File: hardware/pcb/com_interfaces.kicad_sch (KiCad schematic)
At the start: 1 part, among them U4 MAX485E

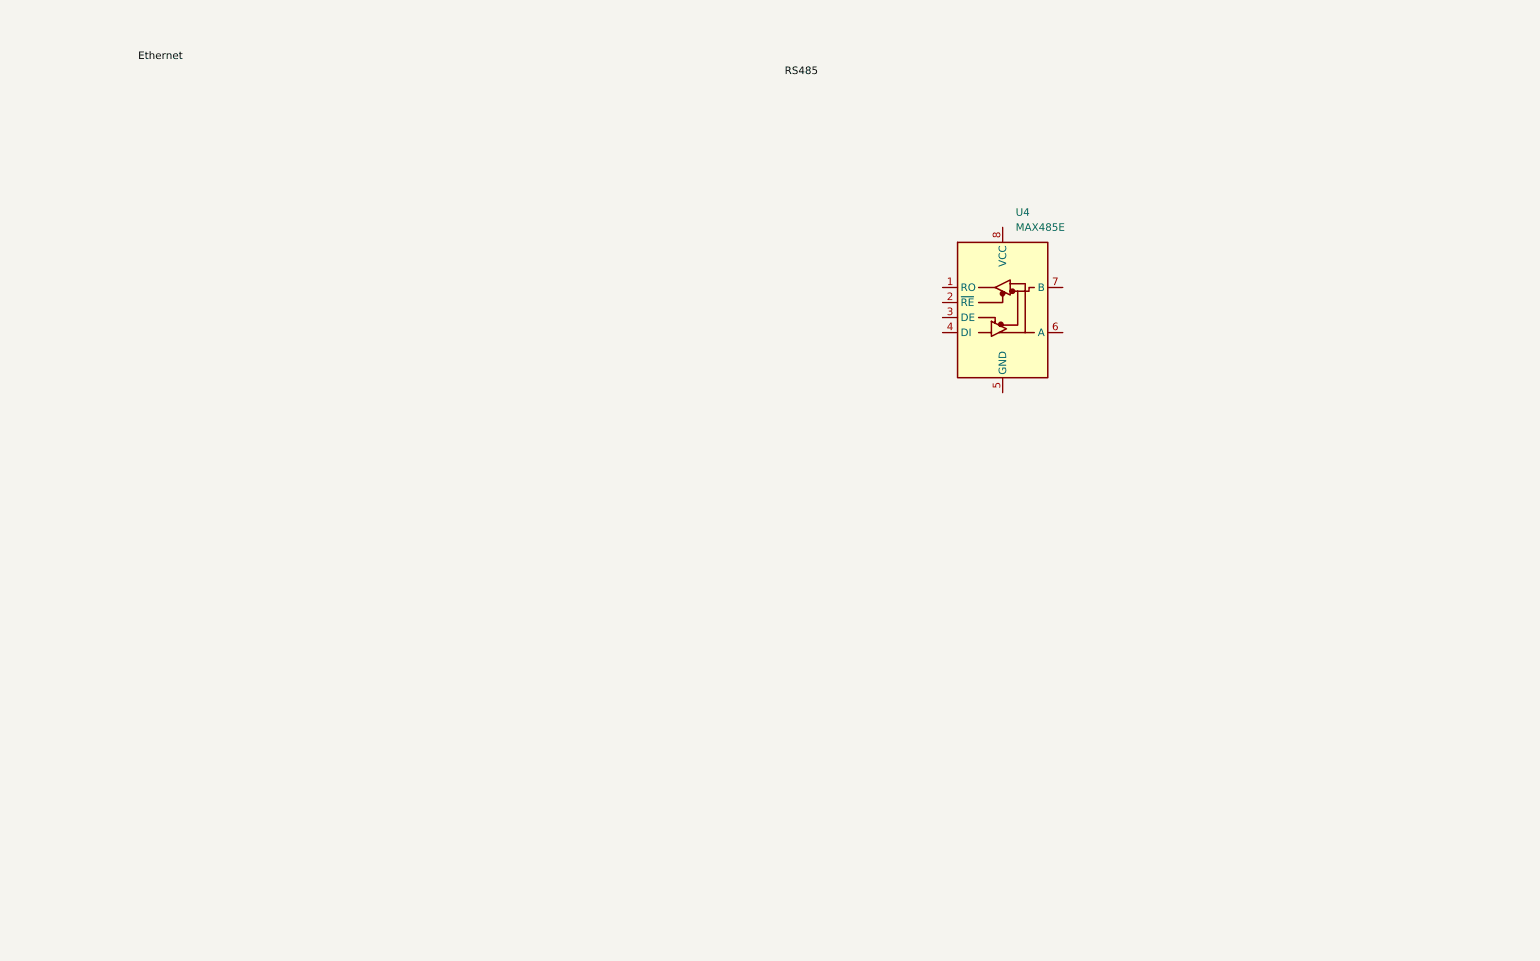
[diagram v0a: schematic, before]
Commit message: draft: Added W5500 Ethernet
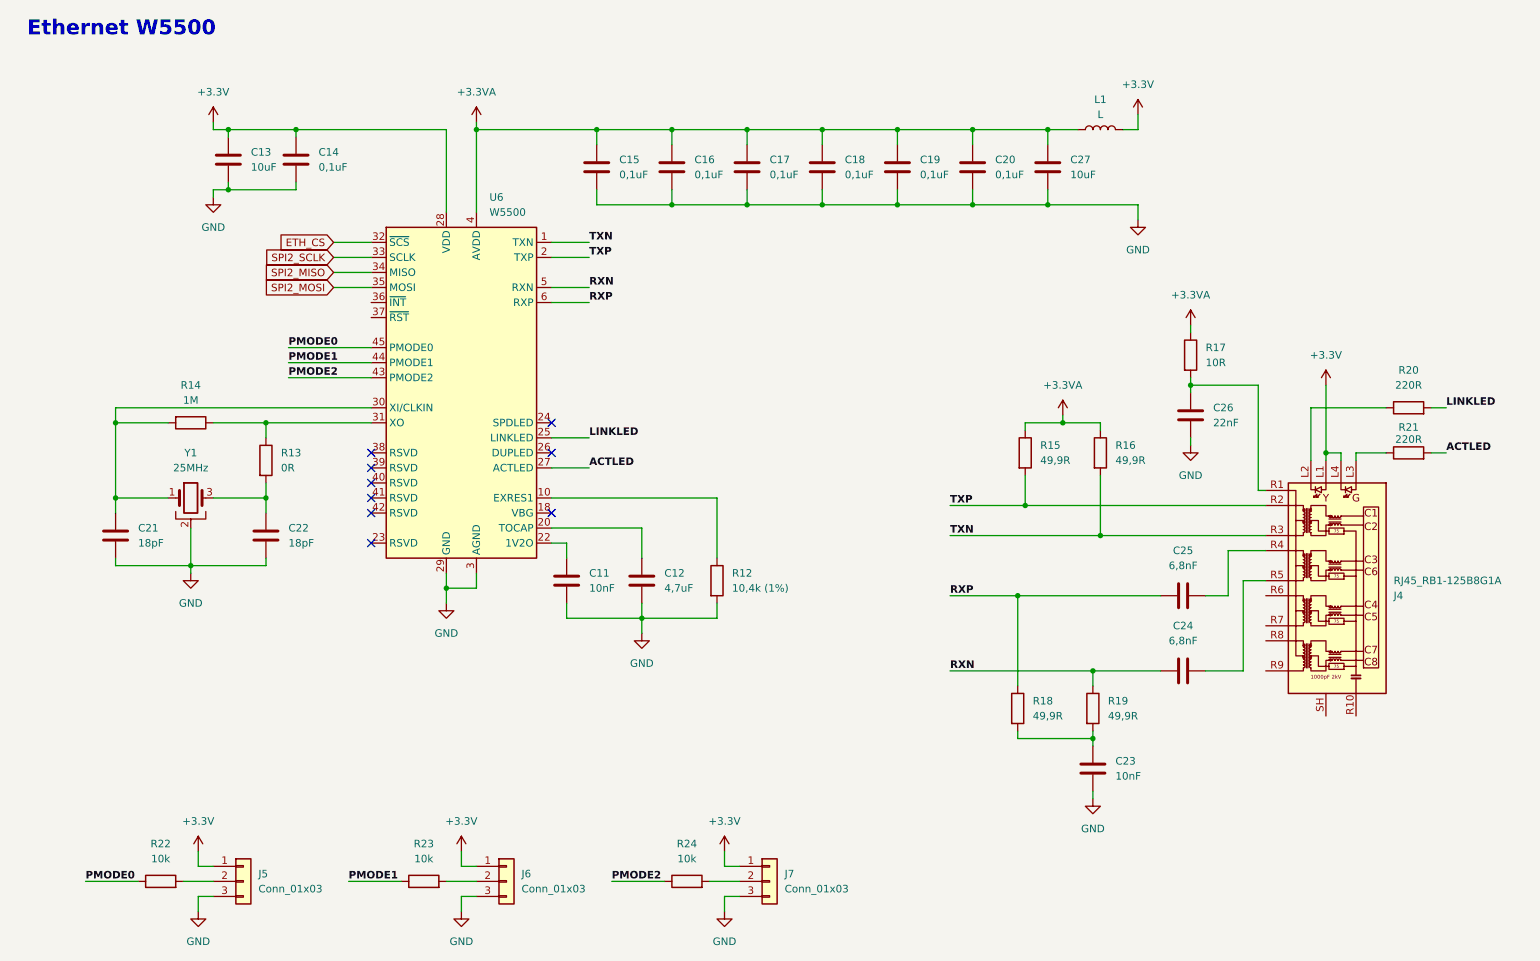
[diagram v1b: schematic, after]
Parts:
- removed U4: MAX485E, symbol Interface_UART:MAX485E
- added C11, C23: 10nF, symbol Device:C
- added C12: 4,7uF, symbol Device:C
- added C13, C27: 10uF, symbol Device:C
- added C14, C15, C16, C17, C18, C19, C20: 0,1uF, symbol Device:C
- added C21, C22: 18pF, symbol Device:C
- added C24, C25: 6,8nF, symbol Device:C
- added C26: 22nF, symbol Device:C
- added J4: RJ45_RB1-125B8G1A, Connector_RJ:RJ45_UDE_RB1-125B8G1A, symbol Connector:RJ45_RB1-125B8G1A
- added J5, J6, J7: Conn_01x03, symbol Connector_Generic:Conn_01x03
- added L1: L, symbol Device:L
- added R12: 10,4k (1%), symbol Device:R
- added R13: 0R, symbol Device:R
- added R14: 1M, symbol Device:R
- added R15, R16, R18, R19: 49,9R, symbol Device:R
- added R17: 10R, symbol Device:R
- added R20, R21: 220R, symbol Device:R
- added R22, R23, R24: 10k, symbol Device:R
- added U6: W5500, Package_QFP:LQFP-48_7x7mm_P0.5mm, symbol Interface_Ethernet:W5500
- added Y1: 25MHz, symbol Device:Crystal_GND2
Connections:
- new net: J6.2 (Pin_2), R23.2
- new net: R12.1, U6.10 (EXRES1)
- new net: C12.1, U6.20 (TOCAP)
- new net: C11.1, U6.22 (1V2O)
- new net: C21.1, R14.2, U6.30 (XI/CLKIN), Y1.1
- new net: R13.1, R14.1, U6.31 (XO)
- new net: C22.1, R13.2, Y1.3
- new net: C23.1, R18.2, R19.2
- new net: J5.2 (Pin_2), R22.2
- new net: J4.L2, R20.1
- new net: C26.1, J4.R1 (CT), R17.2
- new net: J7.2 (Pin_2), R24.2
- new net: C25.2, J4.R4 (TD2+)
- new net: J4.L3, R21.1
- new net: C24.2, J4.R5 (TD2-)
- new net +3.3V: C13.1, C14.1, J4.L1, J4.L4, J5.1 (Pin_1), J6.1 (Pin_1), J7.1 (Pin_1), L1.2, U6.28 (VDD)
- new net +3.3VA: C15.1, C16.1, C17.1, C18.1, C19.1, C20.1, C27.1, L1.1, R15.1, R16.1, R17.1, U6.11 (AVDD), U6.15 (AVDD), U6.17 (AVDD), U6.21 (AVDD), U6.4 (AVDD), U6.8 (AVDD)
- new net ACTLED: R21.2, U6.27 (ACTLED)
- new net ETH_CS: U6.32 (~{SCS})
- new net GND: C11.2, C12.2, C13.2, C14.2, C15.2, C16.2, C17.2, C18.2, C19.2, C20.2, C21.2, C22.2, C23.2, C26.2, C27.2, J5.3 (Pin_3), J6.3 (Pin_3), J7.3 (Pin_3), R12.2, U6.14 (AGND), U6.16 (AGND), U6.19 (AGND), U6.29 (GND), U6.3 (AGND), U6.48 (AGND), U6.9 (AGND), Y1.2
- new net LINKLED: R20.2, U6.25 (LINKLED)
- new net PMODE0: R22.1, U6.45 (PMODE0)
- new net PMODE1: R23.1, U6.44 (PMODE1)
- new net PMODE2: R24.1, U6.43 (PMODE2)
- new net RXN: C24.1, R19.1, U6.5 (RXN)
- new net RXP: C25.1, R18.1, U6.6 (RXP)
- new net SPI2_MISO: U6.34 (MISO)
- new net SPI2_MOSI: U6.35 (MOSI)
- new net SPI2_SCLK: U6.33 (SCLK)
- new net TXN: J4.R3 (TD1-), R16.2, U6.1 (TXN)
- new net TXP: J4.R2 (TD1+), R15.2, U6.2 (TXP)
- no-connect marks 0 -> 9
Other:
- note added: "Ethernet W5500"
- title: (none) -> Ethernet W5500

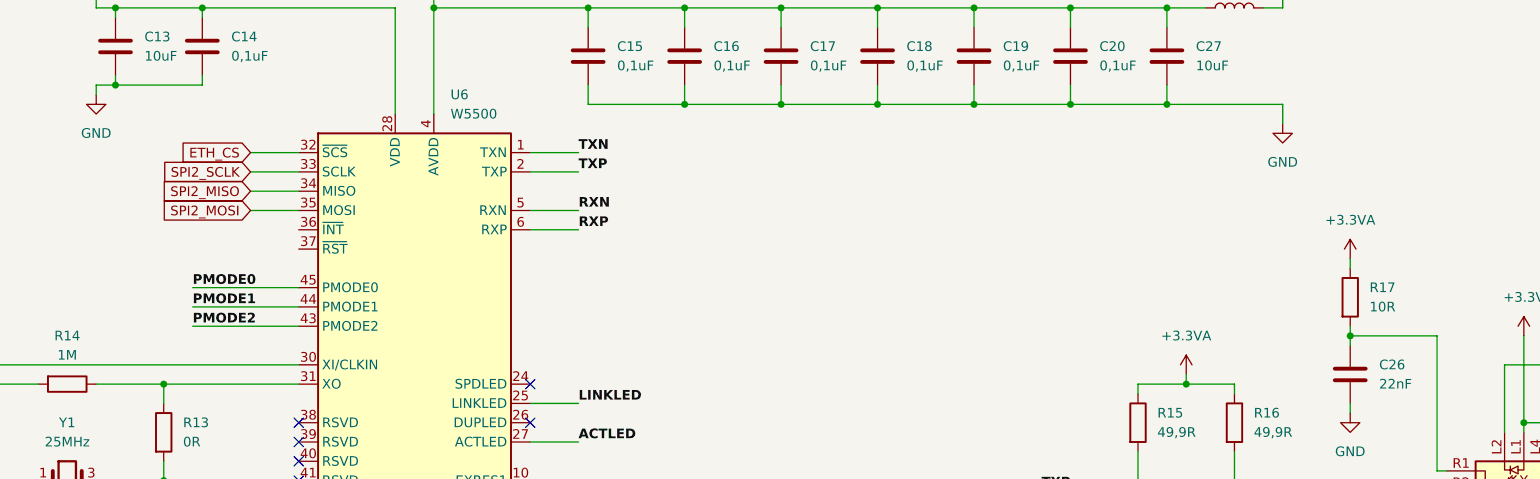
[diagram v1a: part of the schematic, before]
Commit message: draft: Added pin connections to esp32
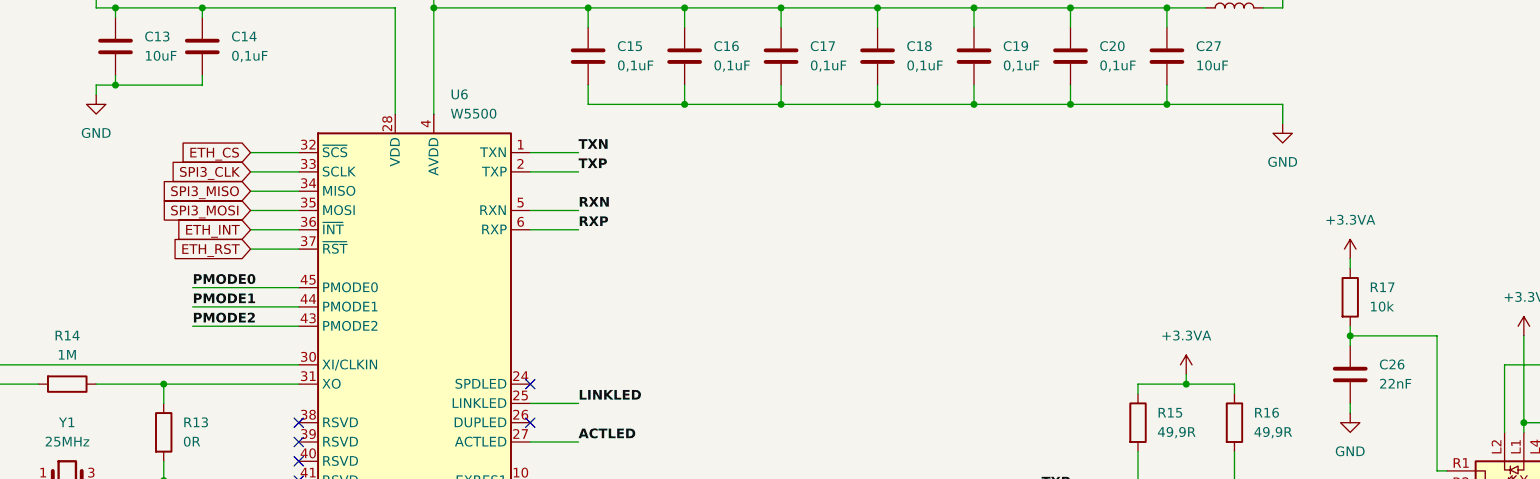
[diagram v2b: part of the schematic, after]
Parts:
- R17: value 10R -> 10k
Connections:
- net ETH_INT: now reaches U6.36 (~{INT})
- net ETH_RST: now reaches U6.37 (~{RST})
- net SPI2_MISO renamed SPI3_MISO
- net SPI2_MOSI renamed SPI3_MOSI
- net SPI2_SCLK renamed SPI3_CLK
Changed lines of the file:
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@@
+	(wire
+		(pts
+			(xy 71.12 72.39) (xy 77.47 72.39)
+		)
+		(stroke
+			(width 0)
+			(type default)
+		)
+	)
 	(wire
 		(pts
@@
 		(pts
 			(xy 128.27 40.64) (xy 128.27 43.18)
+		)
+		(stroke
+			(width 0)
+			(type default)
+		)
+	)
+	(wire
+		(pts
+			(xy 71.12 69.85) (xy 77.47 69.85)
 		)
 		(stroke
@@
 		)
 	)
-	(global_label "SPI2_SCLK"
+	(global_label "SPI3_CLK"
 		(shape input)
 		(at 71.12 62.23 180)
@@
 		)
 		(property "Intersheetrefs" "${INTERSHEET_REFS}"
-			(at 58.0958 62.23 0)
+			(at 59.3053 62.23 0)
 			(effects
 				(font
@@
 		)
 	)
-	(global_label "SPI2_MISO"
+	(global_label "ETH_INT"
 		(shape input)
-		(at 71.12 64.77 180)
+		(at 71.12 69.85 180)
 		(fields_autoplaced yes)
 		(effects
@@
 		)
 		(property "Intersheetrefs" "${INTERSHEET_REFS}"
+			(at 60.8172 69.85 0)
+			(effects
+				(font
+					(size 1.27 1.27)
+				)
+				(justify right)
+				(hide yes)
+			)
+		)
+	)
+	(global_label "SPI3_MISO"
+		(shape input)
+		(at 71.12 64.77 180)
+		(fields_autoplaced yes)
+		(effects
+			(font
+				(size 1.27 1.27)
+			)
+			(justify right)
+		)
+		(property "Intersheetrefs" "${INTERSHEET_REFS}"
 			(at 58.2772 64.77 0)
 			(effects
@@
 		)
 	)
-	(global_label "SPI2_MOSI"
+	(global_label "ETH_RST"
+		(shape input)
+		(at 71.12 72.39 180)
+		(fields_autoplaced yes)
+		(effects
+			(font
+				(size 1.27 1.27)
+			)
+			(justify right)
+		)
+		(property "Intersheetrefs" "${INTERSHEET_REFS}"
+			(at 60.273 72.39 0)
+			(effects
+				(font
+					(size 1.27 1.27)
+				)
+				(justify right)
+				(hide yes)
+			)
+		)
+	)
+	(global_label "SPI3_MOSI"
 		(shape input)
 		(at 71.12 67.31 180)
@@
 			)
 		)
-		(property "Value" "10R"
+		(property "Value" "10k"
 			(at 218.44 80.0099 0)
 			(effects
